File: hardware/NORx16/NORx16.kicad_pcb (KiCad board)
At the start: 2 copper layers, 53.3 x 86.4 mm, 7 parts, among them J1 Left, J2 Right, J3 DBG, J4 Left, J5 Right

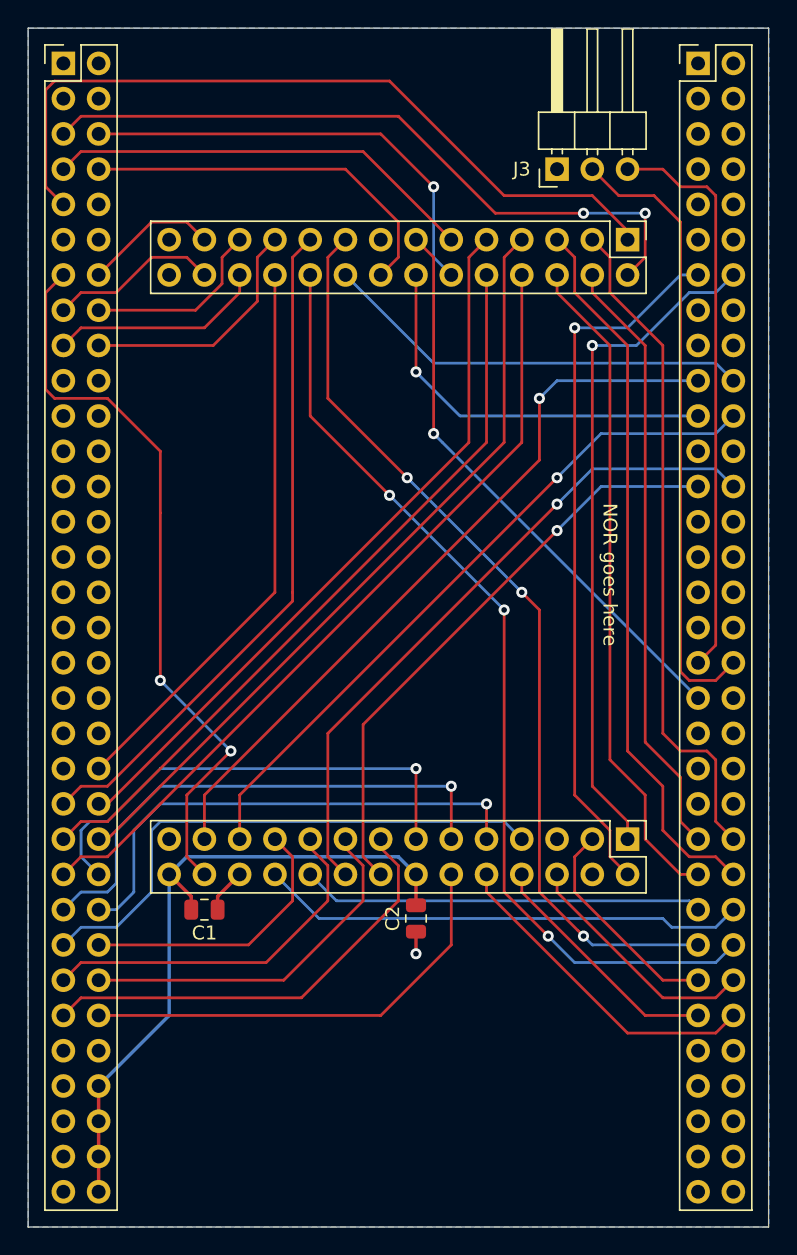
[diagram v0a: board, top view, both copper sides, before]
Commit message: hardware: NOR x16 top to rev.B
+ Added pull-up for ready/busy

+ Modified J3 DBG to break out SWO and GPIO pins
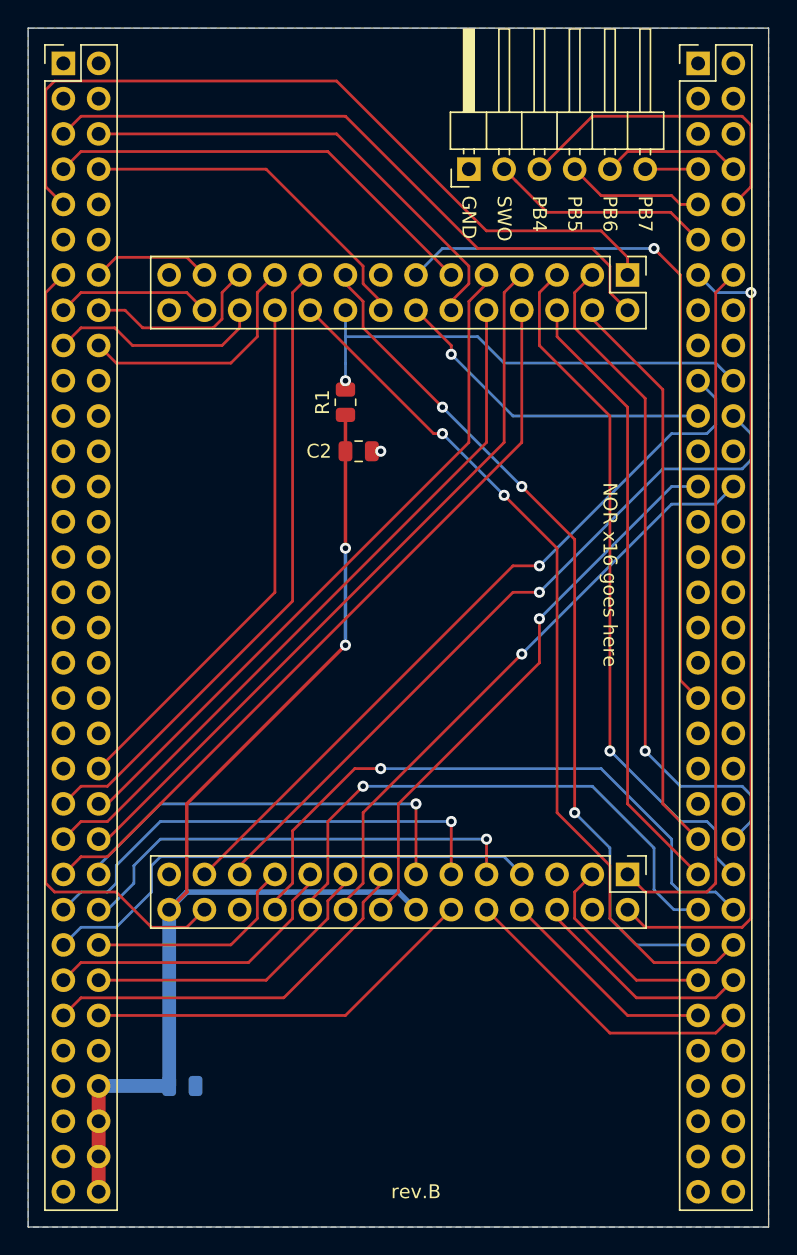
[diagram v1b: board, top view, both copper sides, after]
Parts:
- added R1: 10k, Resistor_SMD:R_0805_2012Metric, F.Cu at (121.9, 100.6)
- C1: moved to B.Cu
- J3: footprint Connector_PinHeader_2.54mm:PinHeader_1x03_P2.54mm_Horizontal -> Connector_PinHeader_2.54mm:PinHeader_1x06_P2.54mm_Horizontal
- moved C2 33.9 mm to (122.9, 104.1), turned to 180 degrees
- moved C1 12.8 mm to (110.2, 149.9)
- moved J3 6.35 mm to (130.8, 83.8)
- moved J4 2.54 mm to (142.2, 91.4)
- moved J5 2.54 mm to (142.2, 134.6)
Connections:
- J1 pad 10: PC13 -> (no net)
- J1 pad 11: PC14 -> (no net)
- J1 pad 12: PC15 -> (no net)
- J1 pad 19: PF6 -> (no net)
- J1 pad 20: PF7 -> (no net)
- J1 pad 21: PF8 -> (no net)
- J1 pad 22: PF9 -> (no net)
- J1 pad 23: PF10 -> (no net)
- J1 pad 24: PC0 -> (no net)
- J1 pad 25: PC1 -> (no net)
- J1 pad 26: PC2 -> (no net)
- J1 pad 27: PC3 -> (no net)
- J1 pad 28: Net-(J1-Pad28) -> (no net)
- J1 pad 29: Net-(J1-Pad29) -> (no net)
- J1 pad 3: PE0 -> (no net)
- J1 pad 32: PA4 -> (no net)
- J1 pad 33: PA5 -> (no net)
- J1 pad 34: PA6 -> (no net)
- J1 pad 35: PA7 -> (no net)
- J1 pad 36: PC4 -> (no net)
- J1 pad 37: PC5 -> (no net)
- J1 pad 38: PB0 -> (no net)
- J1 pad 39: PB1 -> (no net)
- J1 pad 4: PE1 -> (no net)
- J1 pad 40: PB2 -> (no net)
- J1 pad 41: PF11 -> (no net)
- J1 pad 57: PB10 -> (no net)
- J1 pad 58: PB11 -> (no net)
- J2 pad 1: Net-(J2-Pad1) -> (no net)
- J2 pad 12: PG15 -> (no net)
- J2 pad 15: PG12 -> (no net)
- J2 pad 16: PG11 -> (no net)
- J2 pad 17: PG10 -> (no net)
- J2 pad 18: PG9 -> (no net)
- J2 pad 23: PD3 -> (no net)
- J2 pad 24: PD2 -> (no net)
- J2 pad 27: PC12 -> (no net)
- J2 pad 28: PC11 -> (no net)
- J2 pad 29: PC10 -> (no net)
- J2 pad 3: Net-(J2-Pad3) -> (no net)
- J2 pad 30: PA15 -> (no net)
- J2 pad 31: PA14 -> (no net)
- J2 pad 32: PA13 -> (no net)
- J2 pad 33: PA12 -> (no net)
- J2 pad 34: PA11 -> (no net)
- J2 pad 35: PA10 -> (no net)
- J2 pad 36: PA9 -> (no net)
- J2 pad 38: PC9 -> (no net)
- J2 pad 39: PC8 -> (no net)
- J2 pad 40: PC7 -> (no net)
- J2 pad 41: PC6 -> (no net)
- J2 pad 42: PG8 -> (no net)
- J2 pad 43: PG7 -> (no net)
- J2 pad 44: PG6 -> (no net)
- J2 pad 5: PB9 -> (no net)
- J2 pad 57: PB15 -> (no net)
- J2 pad 58: PB14 -> (no net)
- J2 pad 59: PB13 -> (no net)
- J2 pad 6: PB8 -> (no net)
- J2 pad 60: PB12 -> (no net)
- J2 pad 65: Net-(J2-Pad65) -> (no net)
- J3 pad 2: PA9 -> PB3
- J3 pad 3: PA10 -> PB4
- J4 pad 15: Net-(J4-Pad15) -> (no net)
- J4 pad 27: Net-(J4-Pad27) -> (no net)
- J4 pad 28: Net-(J4-Pad28) -> (no net)
- J5 pad 27: Net-(J5-Pad27) -> (no net)
- J5 pad 4: Net-(J5-Pad4) -> (no net)
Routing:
- net PA9: track 44.9 -> 0.00 mm
- net PA10: track 41.3 -> 0.00 mm
- net +3V3: track 49.2 -> 85.1 mm, vias 0 -> 2
- net PB4: track 0.00 -> 23.3 mm
- net PB3: track 0.00 -> 16.1 mm
- net IO1: track 29.0 -> 40.0 mm, vias 0 -> 1
- net IO0: track 35.1 -> 45.9 mm, vias 0 -> 1
- net ~RST: track 41.4 -> 51.6 mm
- net PB6: track 0.00 -> 9.94 mm
- net PB5: track 0.00 -> 9.94 mm
- net A25: track 51.4 -> 59.1 mm
- net A17: track 69.4 -> 63.9 mm, vias 3 -> 2
- net A18: track 66.8 -> 61.4 mm
- net ~WE: track 28.6 -> 23.8 mm
- net IO2: track 48.3 -> 43.9 mm
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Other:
- board text added: "GND"
- board text added: "NOR x16 goes here"
- board text added: "PB4"
- board text added: "PB5"
- board text added: "PB6"
- board text added: "PB7"
- board text added: "SWO"
- board text added: "rev.B"
- board text removed: "NOR goes here"

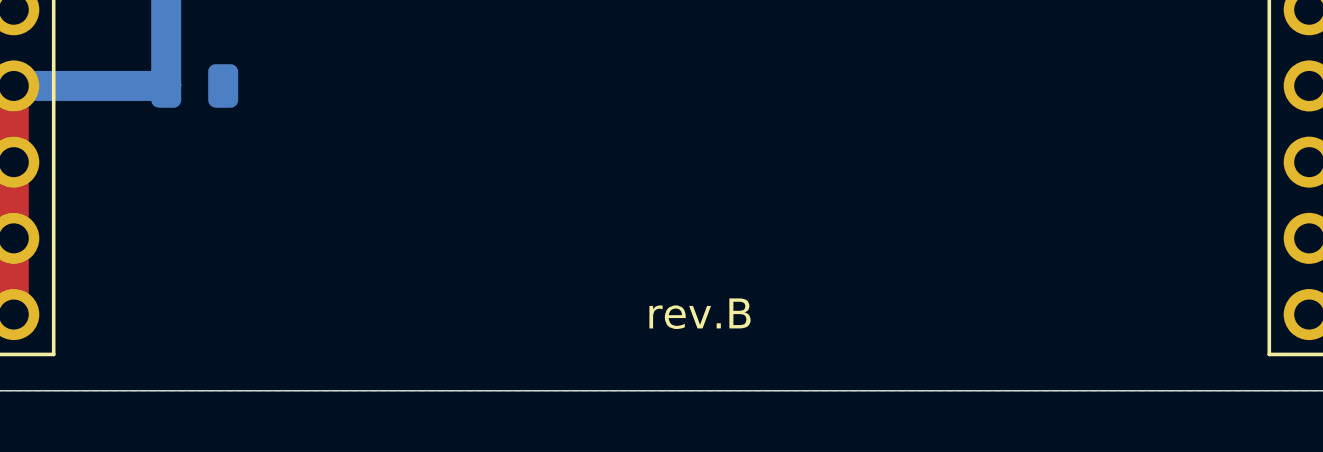
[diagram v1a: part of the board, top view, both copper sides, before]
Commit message: hardware: update top board labels
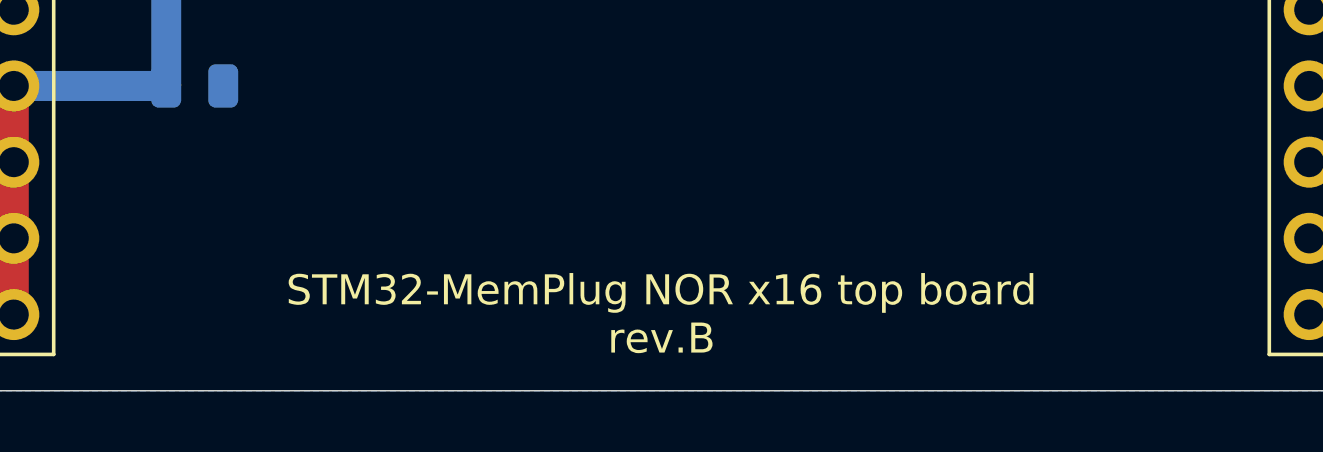
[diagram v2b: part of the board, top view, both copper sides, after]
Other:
- board text added: "STM32-MemPlug NOR x16 top board rev.B"
- board text removed: "rev.B"
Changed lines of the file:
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@@
     (add_net IO8)
     (add_net IO9)
-    (add_net "Net-(J1-Pad28)")
-    (add_net "Net-(J1-Pad29)")
-    (add_net "Net-(J2-Pad1)")
-    (add_net "Net-(J2-Pad3)")
-    (add_net "Net-(J2-Pad65)")
-    (add_net "Net-(J4-Pad15)")
-    (add_net "Net-(J4-Pad27)")
-    (add_net "Net-(J4-Pad28)")
-    (add_net "Net-(J5-Pad27)")
-    (add_net "Net-(J5-Pad4)")
-    (add_net PA10)
-    (add_net PA11)
-    (add_net PA12)
-    (add_net PA13)
-    (add_net PA14)
-    (add_net PA15)
-    (add_net PA4)
-    (add_net PA5)
-    (add_net PA6)
-    (add_net PA7)
-    (add_net PA9)
-    (add_net PB0)
-    (add_net PB1)
-    (add_net PB10)
-    (add_net PB11)
-    (add_net PB12)
-    (add_net PB13)
-    (add_net PB14)
-    (add_net PB15)
-    (add_net PB2)
     (add_net PB3)
     (add_net PB4)
@@
     (add_net PB6)
     (add_net PB7)
-    (add_net PB8)
-    (add_net PB9)
-    (add_net PC0)
-    (add_net PC1)
-    (add_net PC10)
-    (add_net PC11)
-    (add_net PC12)
-    (add_net PC13)
-    (add_net PC14)
-    (add_net PC15)
-    (add_net PC2)
-    (add_net PC3)
-    (add_net PC4)
-    (add_net PC5)
-    (add_net PC6)
-    (add_net PC7)
-    (add_net PC8)
-    (add_net PC9)
-    (add_net PD2)
-    (add_net PD3)
-    (add_net PE0)
-    (add_net PE1)
-    (add_net PF10)
-    (add_net PF11)
-    (add_net PF6)
-    (add_net PF7)
-    (add_net PF8)
-    (add_net PF9)
-    (add_net PG10)
-    (add_net PG11)
-    (add_net PG12)
-    (add_net PG15)
-    (add_net PG6)
-    (add_net PG7)
-    (add_net PG8)
-    (add_net PG9)
     (add_net R~B)
     (add_net ~CE)
@@
     (fp_text value 10k (at 0 1.65 90) (layer F.Fab)
       (effects (font (size 1 1) (thickness 0.15)))
-    )
-    (fp_text user %R (at 0 0 90) (layer F.Fab)
-      (effects (font (size 0.5 0.5) (thickness 0.08)))
     )
     (fp_line (start -1 0.625) (end -1 -0.625) (layer F.Fab) (width 0.1))
@@
     (fp_line (start 1.68 -0.95) (end 1.68 0.95) (layer F.CrtYd) (width 0.05))
     (fp_line (start 1.68 0.95) (end -1.68 0.95) (layer F.CrtYd) (width 0.05))
+    (fp_text user %R (at 0 0 90) (layer F.Fab)
+      (effects (font (size 0.5 0.5) (thickness 0.08)))
+    )
     (pad 2 smd roundrect (at 0.9125 0 90) (size 1.025 1.4) (layers F.Cu F.Paste F.Mask) (roundrect_rratio 0.243902)
       (net 12 R~B))
@@
     )
     (fp_text value DBG (at 4.385 14.97 90) (layer F.Fab)
-      (effects (font (size 1 1) (thickness 0.15)))
-    )
-    (fp_text user %R (at 2.77 6.35) (layer F.Fab)
       (effects (font (size 1 1) (thickness 0.15)))
     )
@@
     (fp_line (start 10.55 14.5) (end 10.55 -1.8) (layer F.CrtYd) (width 0.05))
     (fp_line (start 10.55 -1.8) (end -1.8 -1.8) (layer F.CrtYd) (width 0.05))
+    (fp_text user %R (at 2.77 6.35) (layer F.Fab)
+      (effects (font (size 1 1) (thickness 0.15)))
+    )
     (pad 6 thru_hole oval (at 0 12.7 90) (size 1.7 1.7) (drill 1) (layers *.Cu *.Mask)
       (net 38 PB7))
@@
     )
     (fp_text value Right (at 1.27 83.61) (layer F.Fab)
-      (effects (font (size 1 1) (thickness 0.15)))
-    )
-    (fp_text user %R (at 1.27 40.64 90) (layer F.Fab)
       (effects (font (size 1 1) (thickness 0.15)))
     )
@@
     (fp_line (start 4.35 83.05) (end 4.35 -1.8) (layer F.CrtYd) (width 0.05))
     (fp_line (start 4.35 -1.8) (end -1.8 -1.8) (layer F.CrtYd) (width 0.05))
+    (fp_text user %R (at 1.27 40.64 90) (layer F.Fab)
+      (effects (font (size 1 1) (thickness 0.15)))
+    )
     (pad 66 thru_hole oval (at 2.54 81.28) (size 1.7 1.7) (drill 1) (layers *.Cu *.Mask)
       (net 2 GND))
@@
       (effects (font (size 1 1) (thickness 0.15)))
     )
-    (fp_text user %R (at 1.27 40.64 90) (layer F.Fab)
-      (effects (font (size 1 1) (thickness 0.15)))
-    )
     (fp_line (start 0 -1.27) (end 3.81 -1.27) (layer F.Fab) (width 0.1))
     (fp_line (start 3.81 -1.27) (end 3.81 82.55) (layer F.Fab) (width 0.1))
@@
     (fp_line (start 4.35 83.05) (end 4.35 -1.8) (layer F.CrtYd) (width 0.05))
     (fp_line (start 4.35 -1.8) (end -1.8 -1.8) (layer F.CrtYd) (width 0.05))
+    (fp_text user %R (at 1.27 40.64 90) (layer F.Fab)
+      (effects (font (size 1 1) (thickness 0.15)))
+    )
     (pad 66 thru_hole oval (at 2.54 81.28) (size 1.7 1.7) (drill 1) (layers *.Cu *.Mask)
       (net 1 +3V3))
@@
     (effects (font (size 1 1) (thickness 0.15)) (justify left))
   )
-  (gr_text rev.B (at 127 157.48) (layer F.SilkS)
+  (gr_text "STM32-MemPlug NOR x16 top board\nrev.B" (at 125.73 157.48) (layer F.SilkS)
     (effects (font (size 1 1) (thickness 0.15)))
   )

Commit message: refreshed carrier boards and added missing symbol libs
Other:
- board text added: "DBG1"
- board text added: "DBG2"
- board text added: "DBG3"
- board text added: "DBG4"
- board text removed: "PB4"
- board text removed: "PB5"
- board text removed: "PB6"
- board text removed: "PB7"
